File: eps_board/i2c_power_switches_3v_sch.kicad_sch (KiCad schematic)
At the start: 10 parts, among them U38 MCP23017T-E/SS

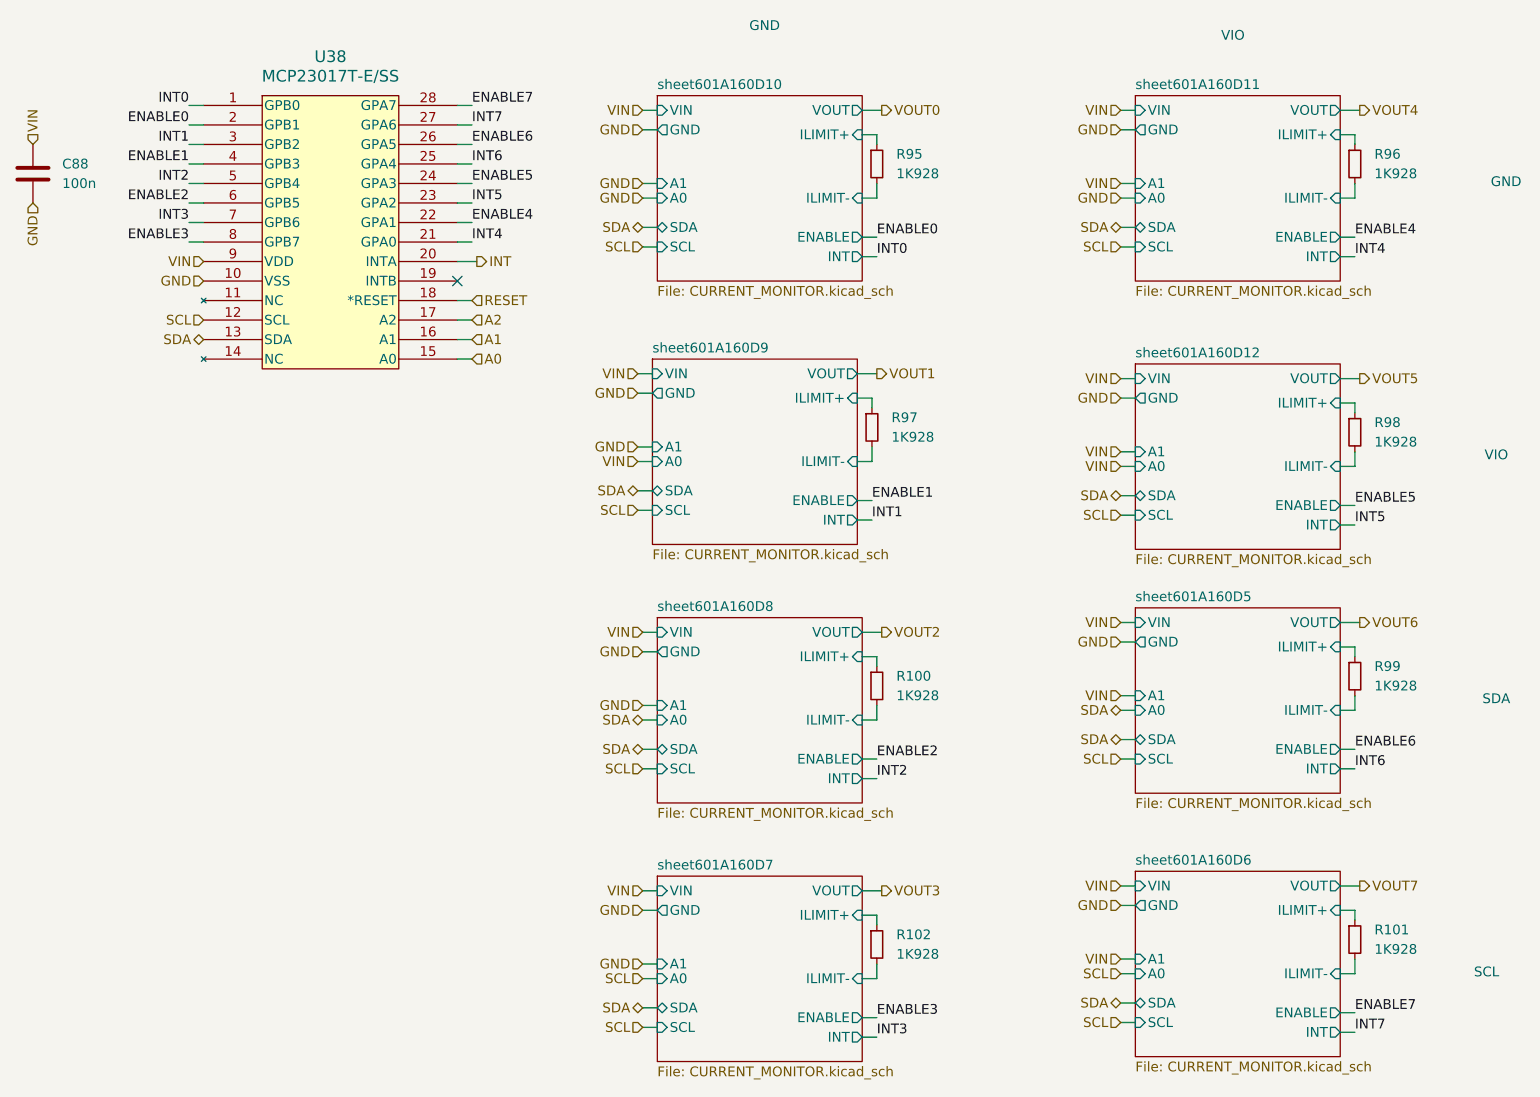
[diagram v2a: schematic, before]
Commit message: light sensors with i2c multiplexers for AVI board. i2c amp/volt meter for attitude control coils
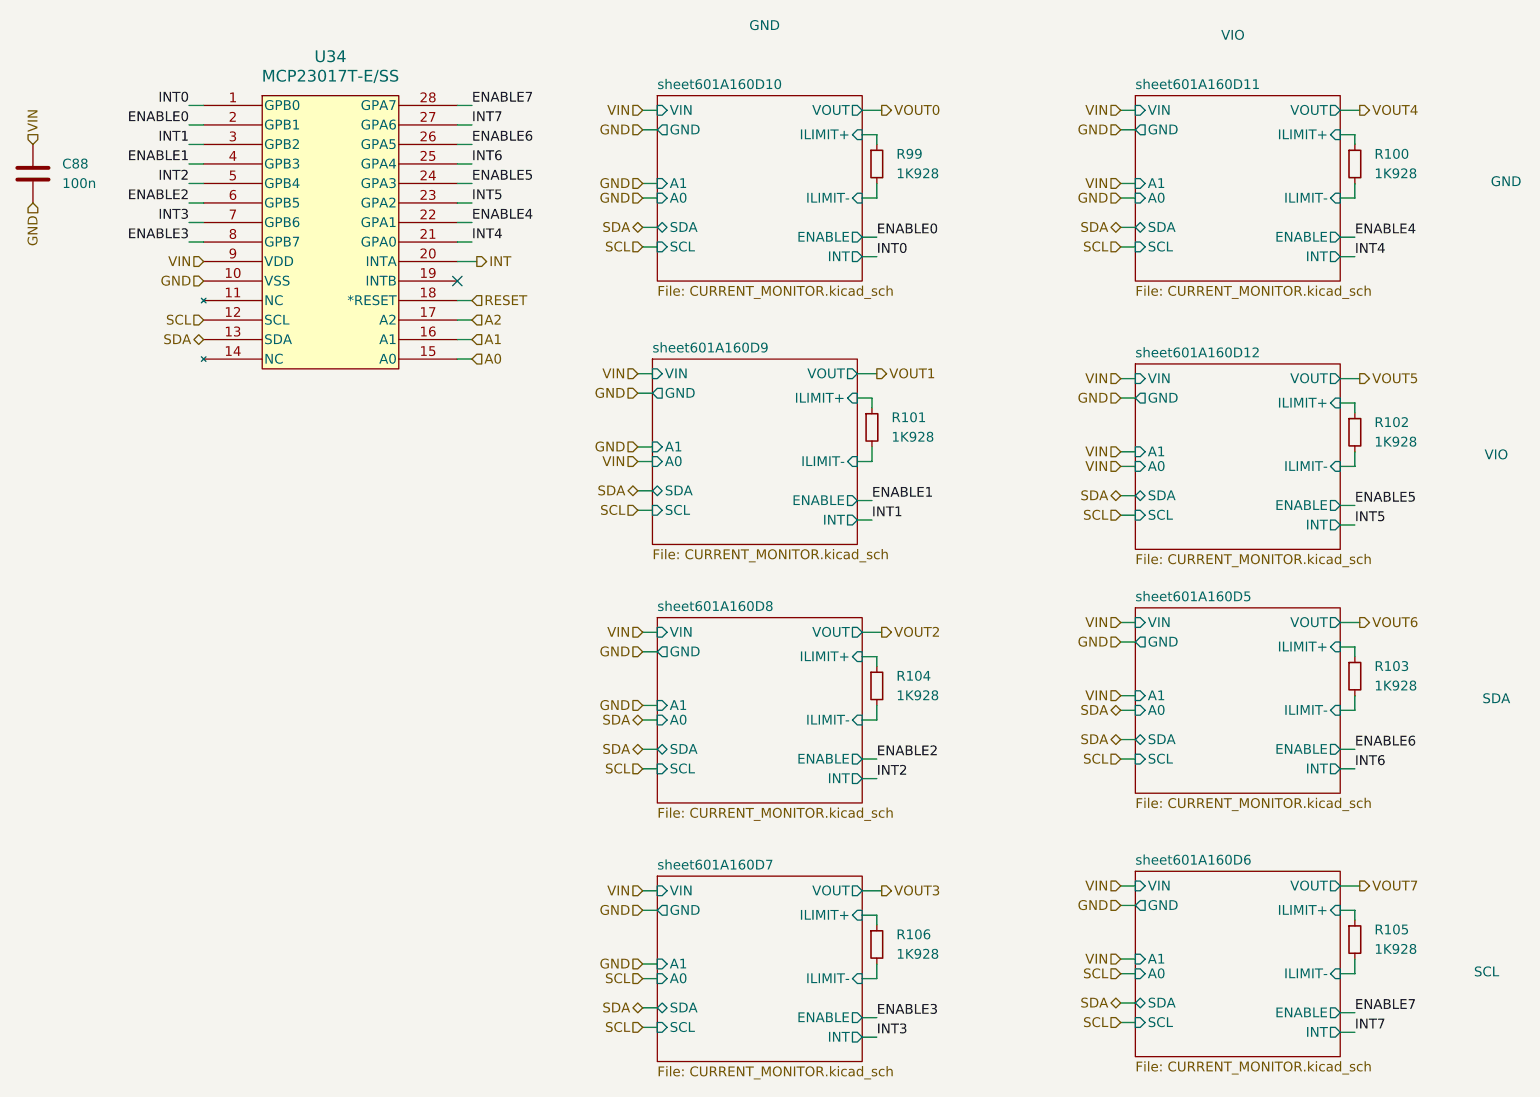
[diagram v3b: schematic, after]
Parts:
- renumbered R96 to R100, R97 to R101, R98 to R102, R99 to R103, R100 to R104, R101 to R105, R102 to R106, R95 to R99, U38 to U34
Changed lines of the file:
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@@
 		(dnp no)
 		(fields_autoplaced yes)
-		(property "Reference" "U38"
+		(property "Reference" "U34"
 			(at 60.325 27.94 0)
 			(effects
@@
 			(project ""
 				(path "/05170af6-30ef-4c3a-b972-f098085da1bc/365e30aa-57e3-49e2-b136-6964bfe03313"
-					(reference "U38")
-					(unit 1)
-				)
-				(path "/05170af6-30ef-4c3a-b972-f098085da1bc/87d4360e-0b9f-4926-a66e-357599f9c0d1"
-					(reference "U58")
+					(reference "U34")
+					(unit 1)
+				)
+				(path "/05170af6-30ef-4c3a-b972-f098085da1bc/87d4360e-0b9f-4926-a66e-357599f9c0d1"
+					(reference "U54")
 					(unit 1)
 				)
@@
 		(dnp no)
 		(fields_autoplaced yes)
-		(property "Reference" "R99"
+		(property "Reference" "R103"
 			(at 196.215 107.3149 0)
 			(effects
@@
 			(project "EPS"
 				(path "/05170af6-30ef-4c3a-b972-f098085da1bc/365e30aa-57e3-49e2-b136-6964bfe03313"
-					(reference "R99")
-					(unit 1)
-				)
-				(path "/05170af6-30ef-4c3a-b972-f098085da1bc/87d4360e-0b9f-4926-a66e-357599f9c0d1"
-					(reference "R139")
+					(reference "R103")
+					(unit 1)
+				)
+				(path "/05170af6-30ef-4c3a-b972-f098085da1bc/87d4360e-0b9f-4926-a66e-357599f9c0d1"
+					(reference "R140")
 					(unit 1)
 				)
@@
 		(dnp no)
 		(fields_autoplaced yes)
-		(property "Reference" "R98"
+		(property "Reference" "R102"
 			(at 196.215 75.5649 0)
 			(effects
@@
 			(project "EPS"
 				(path "/05170af6-30ef-4c3a-b972-f098085da1bc/365e30aa-57e3-49e2-b136-6964bfe03313"
-					(reference "R98")
-					(unit 1)
-				)
-				(path "/05170af6-30ef-4c3a-b972-f098085da1bc/87d4360e-0b9f-4926-a66e-357599f9c0d1"
-					(reference "R138")
+					(reference "R102")
+					(unit 1)
+				)
+				(path "/05170af6-30ef-4c3a-b972-f098085da1bc/87d4360e-0b9f-4926-a66e-357599f9c0d1"
+					(reference "R139")
 					(unit 1)
 				)
@@
 		(dnp no)
 		(fields_autoplaced yes)
-		(property "Reference" "R100"
+		(property "Reference" "R104"
 			(at 133.985 108.5849 0)
 			(effects
@@
 			(project "EPS"
 				(path "/05170af6-30ef-4c3a-b972-f098085da1bc/365e30aa-57e3-49e2-b136-6964bfe03313"
-					(reference "R100")
-					(unit 1)
-				)
-				(path "/05170af6-30ef-4c3a-b972-f098085da1bc/87d4360e-0b9f-4926-a66e-357599f9c0d1"
-					(reference "R140")
+					(reference "R104")
+					(unit 1)
+				)
+				(path "/05170af6-30ef-4c3a-b972-f098085da1bc/87d4360e-0b9f-4926-a66e-357599f9c0d1"
+					(reference "R141")
 					(unit 1)
 				)
@@
 		(dnp no)
 		(fields_autoplaced yes)
-		(property "Reference" "R101"
+		(property "Reference" "R105"
 			(at 196.215 141.6049 0)
 			(effects
@@
 			(project "EPS"
 				(path "/05170af6-30ef-4c3a-b972-f098085da1bc/365e30aa-57e3-49e2-b136-6964bfe03313"
-					(reference "R101")
-					(unit 1)
-				)
-				(path "/05170af6-30ef-4c3a-b972-f098085da1bc/87d4360e-0b9f-4926-a66e-357599f9c0d1"
-					(reference "R141")
+					(reference "R105")
+					(unit 1)
+				)
+				(path "/05170af6-30ef-4c3a-b972-f098085da1bc/87d4360e-0b9f-4926-a66e-357599f9c0d1"
+					(reference "R142")
 					(unit 1)
 				)
@@
 		(dnp no)
 		(fields_autoplaced yes)
-		(property "Reference" "R95"
+		(property "Reference" "R99"
 			(at 133.985 40.6399 0)
 			(effects
@@
 			(project "EPS"
 				(path "/05170af6-30ef-4c3a-b972-f098085da1bc/365e30aa-57e3-49e2-b136-6964bfe03313"
-					(reference "R95")
-					(unit 1)
-				)
-				(path "/05170af6-30ef-4c3a-b972-f098085da1bc/87d4360e-0b9f-4926-a66e-357599f9c0d1"
-					(reference "R135")
+					(reference "R99")
+					(unit 1)
+				)
+				(path "/05170af6-30ef-4c3a-b972-f098085da1bc/87d4360e-0b9f-4926-a66e-357599f9c0d1"
+					(reference "R136")
 					(unit 1)
 				)
@@
 		(dnp no)
 		(fields_autoplaced yes)
-		(property "Reference" "R102"
+		(property "Reference" "R106"
 			(at 133.985 142.2399 0)
 			(effects
@@
 			(project "EPS"
 				(path "/05170af6-30ef-4c3a-b972-f098085da1bc/365e30aa-57e3-49e2-b136-6964bfe03313"
-					(reference "R102")
-					(unit 1)
-				)
-				(path "/05170af6-30ef-4c3a-b972-f098085da1bc/87d4360e-0b9f-4926-a66e-357599f9c0d1"
-					(reference "R142")
+					(reference "R106")
+					(unit 1)
+				)
+				(path "/05170af6-30ef-4c3a-b972-f098085da1bc/87d4360e-0b9f-4926-a66e-357599f9c0d1"
+					(reference "R143")
 					(unit 1)
 				)
@@
 		(dnp no)
 		(fields_autoplaced yes)
-		(property "Reference" "R97"
+		(property "Reference" "R101"
 			(at 133.35 74.9299 0)
 			(effects
@@
 			(project "EPS"
 				(path "/05170af6-30ef-4c3a-b972-f098085da1bc/365e30aa-57e3-49e2-b136-6964bfe03313"
-					(reference "R97")
-					(unit 1)
-				)
-				(path "/05170af6-30ef-4c3a-b972-f098085da1bc/87d4360e-0b9f-4926-a66e-357599f9c0d1"
-					(reference "R137")
+					(reference "R101")
+					(unit 1)
+				)
+				(path "/05170af6-30ef-4c3a-b972-f098085da1bc/87d4360e-0b9f-4926-a66e-357599f9c0d1"
+					(reference "R138")
 					(unit 1)
 				)
@@
 		(dnp no)
 		(fields_autoplaced yes)
-		(property "Reference" "R96"
+		(property "Reference" "R100"
 			(at 196.215 40.6399 0)
 			(effects
@@
 			(project "EPS"
 				(path "/05170af6-30ef-4c3a-b972-f098085da1bc/365e30aa-57e3-49e2-b136-6964bfe03313"
-					(reference "R96")
-					(unit 1)
-				)
-				(path "/05170af6-30ef-4c3a-b972-f098085da1bc/87d4360e-0b9f-4926-a66e-357599f9c0d1"
-					(reference "R136")
-					(unit 1)
-				)
+					(reference "R100")
+					(unit 1)
+				)
+				(path "/05170af6-30ef-4c3a-b972-f098085da1bc/87d4360e-0b9f-4926-a66e-357599f9c0d1"
+					(reference "R137")
+					(unit 1)
+				)

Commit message: interim checkin for EPS BOM
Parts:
- C88: value 100n -> 100nF; Manufacturer (none) -> Murata; Part Number (none) -> GRM155R61E104KA87D; Tolerance (none) -> 10; Voltage (none) -> 25
- R100, R101, R102, R103, R104, R105, R106, R99: footprint Resistor_SMD:R_0603_1608Metric_Pad0.98x0.95mm_HandSolder -> Resistor_SMD:R_0402_1005Metric_Pad0.72x0.64mm_HandSolder; Manufacturer (none) -> YAGEO; Part Number (none) -> RC0402FR-071K928L; Tolerance (none) -> 1
- U34: symbol Project:MCP23017T-E_SS -> Common:MCP23017T-E_SS

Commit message: complete BOM assignment for EPS, next step circular check and deep dives
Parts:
- U34: Manufacturer (none) -> Microchip; Part Number (none) -> MCP23017T-E/SS
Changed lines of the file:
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@@
 			)
 		)
-		(property "Datasheet" "MCP23017T-E/SS"
+		(property "Datasheet" "https://ww1.microchip.com/downloads/aemDocuments/documents/APID/ProductDocuments/DataSheets/MCP23017-Data-Sheet-DS20001952.pdf"
 			(at 43.815 34.29 0)
 			(effects
@@
 			(effects
 				(font
+					(size 1.27 1.27)
+				)
+				(hide yes)
+			)
+		)
+		(property "Manufacturer" "Microchip"
+			(at 27.305 34.29 0)
+			(effects
+				(font
+					(size 1.27 1.27)
+				)
+				(hide yes)
+			)
+		)
+		(property "Part Number" "MCP23017T-E/SS"
+			(at 27.305 34.29 0)
+			(effects
+				(font

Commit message: add decorations and labels to PCBs part 2
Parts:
- R100, R101, R102, R103, R104, R105, R106, R99: footprint Resistor_SMD:R_0402_1005Metric_Pad0.72x0.64mm_HandSolder -> Resistor_SMD:R_0603_1608Metric_Pad0.98x0.95mm_HandSolder; Part Number RC0402FR-071K928L -> RC0603FR-071K928L
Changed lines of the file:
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@@
 			)
 		)
-		(property "Footprint" "Resistor_SMD:R_0402_1005Metric_Pad0.72x0.64mm_HandSolder"
+		(property "Footprint" "Resistor_SMD:R_0603_1608Metric_Pad0.98x0.95mm_HandSolder"
 			(at 193.675 108.585 0)
 			(effects
@@
 			)
 		)
-		(property "Part Number" "RC0402FR-071K928L"
+		(property "Part Number" "RC0603FR-071K928L"
 			(at 193.675 108.585 0)
 			(effects
@@
 			)
 		)
-		(property "Footprint" "Resistor_SMD:R_0402_1005Metric_Pad0.72x0.64mm_HandSolder"
+		(property "Footprint" "Resistor_SMD:R_0603_1608Metric_Pad0.98x0.95mm_HandSolder"
 			(at 193.675 76.835 0)
 			(effects
@@
 			)
 		)
-		(property "Part Number" "RC0402FR-071K928L"
+		(property "Part Number" "RC0603FR-071K928L"
 			(at 193.675 76.835 0)
 			(effects
@@
 			)
 		)
-		(property "Footprint" "Resistor_SMD:R_0402_1005Metric_Pad0.72x0.64mm_HandSolder"
+		(property "Footprint" "Resistor_SMD:R_0603_1608Metric_Pad0.98x0.95mm_HandSolder"
 			(at 131.445 109.855 0)
 			(effects
@@
 			)
 		)
-		(property "Part Number" "RC0402FR-071K928L"
+		(property "Part Number" "RC0603FR-071K928L"
 			(at 131.445 109.855 0)
 			(effects
@@
 			)
 		)
-		(property "Footprint" "Resistor_SMD:R_0402_1005Metric_Pad0.72x0.64mm_HandSolder"
+		(property "Footprint" "Resistor_SMD:R_0603_1608Metric_Pad0.98x0.95mm_HandSolder"
 			(at 193.675 142.875 0)
 			(effects
@@
 			)
 		)
-		(property "Part Number" "RC0402FR-071K928L"
+		(property "Part Number" "RC0603FR-071K928L"
 			(at 193.675 142.875 0)
 			(effects
@@
 			)
 		)
-		(property "Footprint" "Resistor_SMD:R_0402_1005Metric_Pad0.72x0.64mm_HandSolder"
+		(property "Footprint" "Resistor_SMD:R_0603_1608Metric_Pad0.98x0.95mm_HandSolder"
 			(at 131.445 41.91 0)
 			(effects
@@
 			)
 		)
-		(property "Part Number" "RC0402FR-071K928L"
+		(property "Part Number" "RC0603FR-071K928L"
 			(at 131.445 41.91 0)
 			(effects
@@
 			)
 		)
-		(property "Footprint" "Resistor_SMD:R_0402_1005Metric_Pad0.72x0.64mm_HandSolder"
+		(property "Footprint" "Resistor_SMD:R_0603_1608Metric_Pad0.98x0.95mm_HandSolder"
 			(at 131.445 143.51 0)
 			(effects
@@
 			)
 		)
-		(property "Part Number" "RC0402FR-071K928L"
+		(property "Part Number" "RC0603FR-071K928L"
 			(at 131.445 143.51 0)
 			(effects
@@
 			)
 		)
-		(property "Footprint" "Resistor_SMD:R_0402_1005Metric_Pad0.72x0.64mm_HandSolder"
+		(property "Footprint" "Resistor_SMD:R_0603_1608Metric_Pad0.98x0.95mm_HandSolder"
 			(at 130.81 76.2 0)
 			(effects
@@
 			)
 		)
-		(property "Part Number" "RC0402FR-071K928L"
+		(property "Part Number" "RC0603FR-071K928L"
 			(at 130.81 76.2 0)
 			(effects
@@
 			)
 		)
-		(property "Footprint" "Resistor_SMD:R_0402_1005Metric_Pad0.72x0.64mm_HandSolder"
+		(property "Footprint" "Resistor_SMD:R_0603_1608Metric_Pad0.98x0.95mm_HandSolder"
 			(at 193.675 41.91 0)
 			(effects
@@
 			)
 		)
-		(property "Part Number" "RC0402FR-071K928L"
+		(property "Part Number" "RC0603FR-071K928L"
 			(at 193.675 41.91 0)
 			(effects
